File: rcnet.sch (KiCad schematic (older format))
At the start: 19 parts

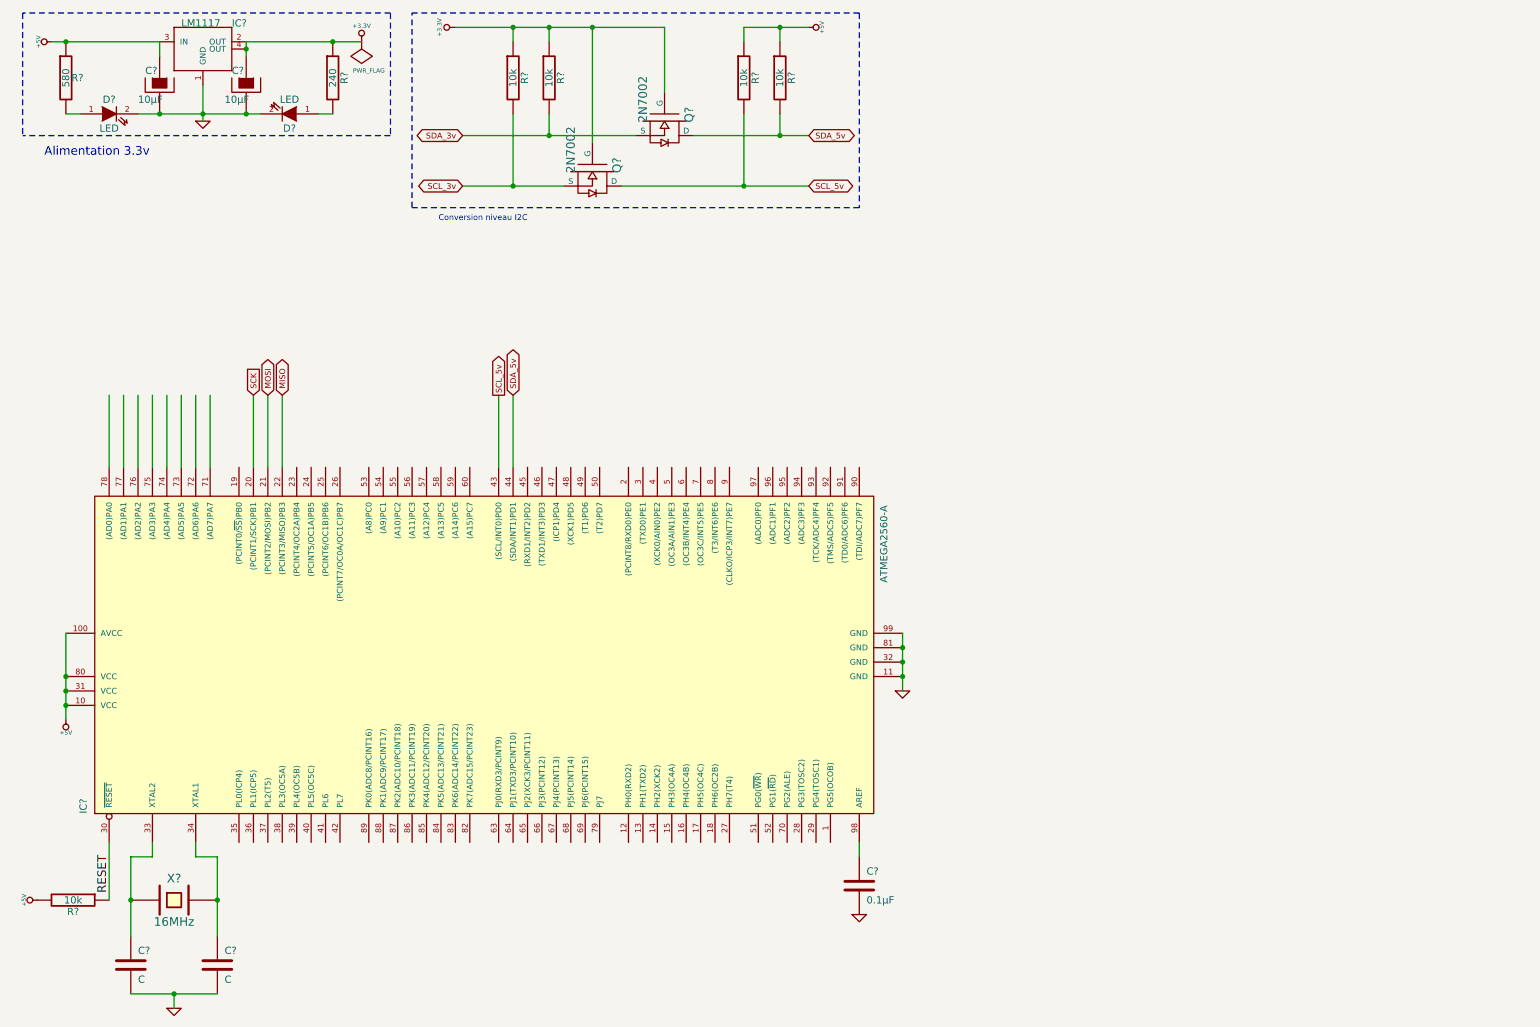
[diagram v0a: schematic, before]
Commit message: Ajout des capteurs I2C et cablage des MPU6050 et MS5611
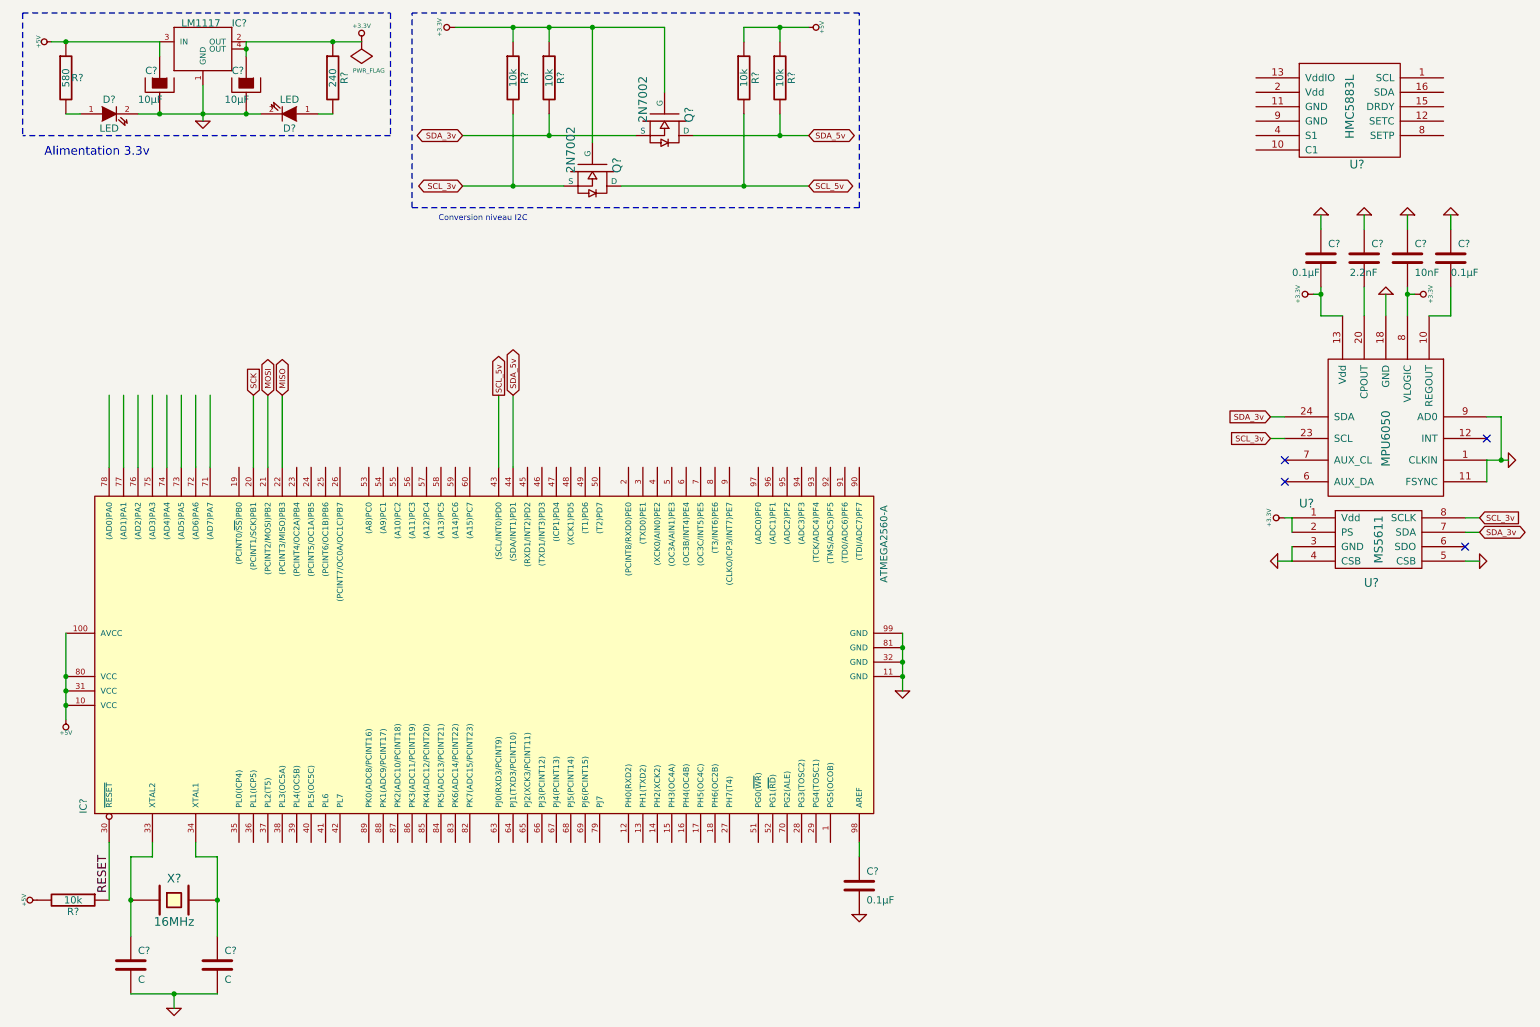
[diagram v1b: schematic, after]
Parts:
- added C?: 10nF, symbol C
- added C? (x2): 0.1µF, symbol C
- added C?: 2.2nF, symbol C
- added U?: HMC5883L, symbol HMC5883L
- added U?: MPU6050, symbol MPU6050
- added U?: MS5611, symbol MS5611
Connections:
- wire segments 49 -> 75
- no-connect marks 0 -> 4

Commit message: Fin d'ajout capteurs I2C.
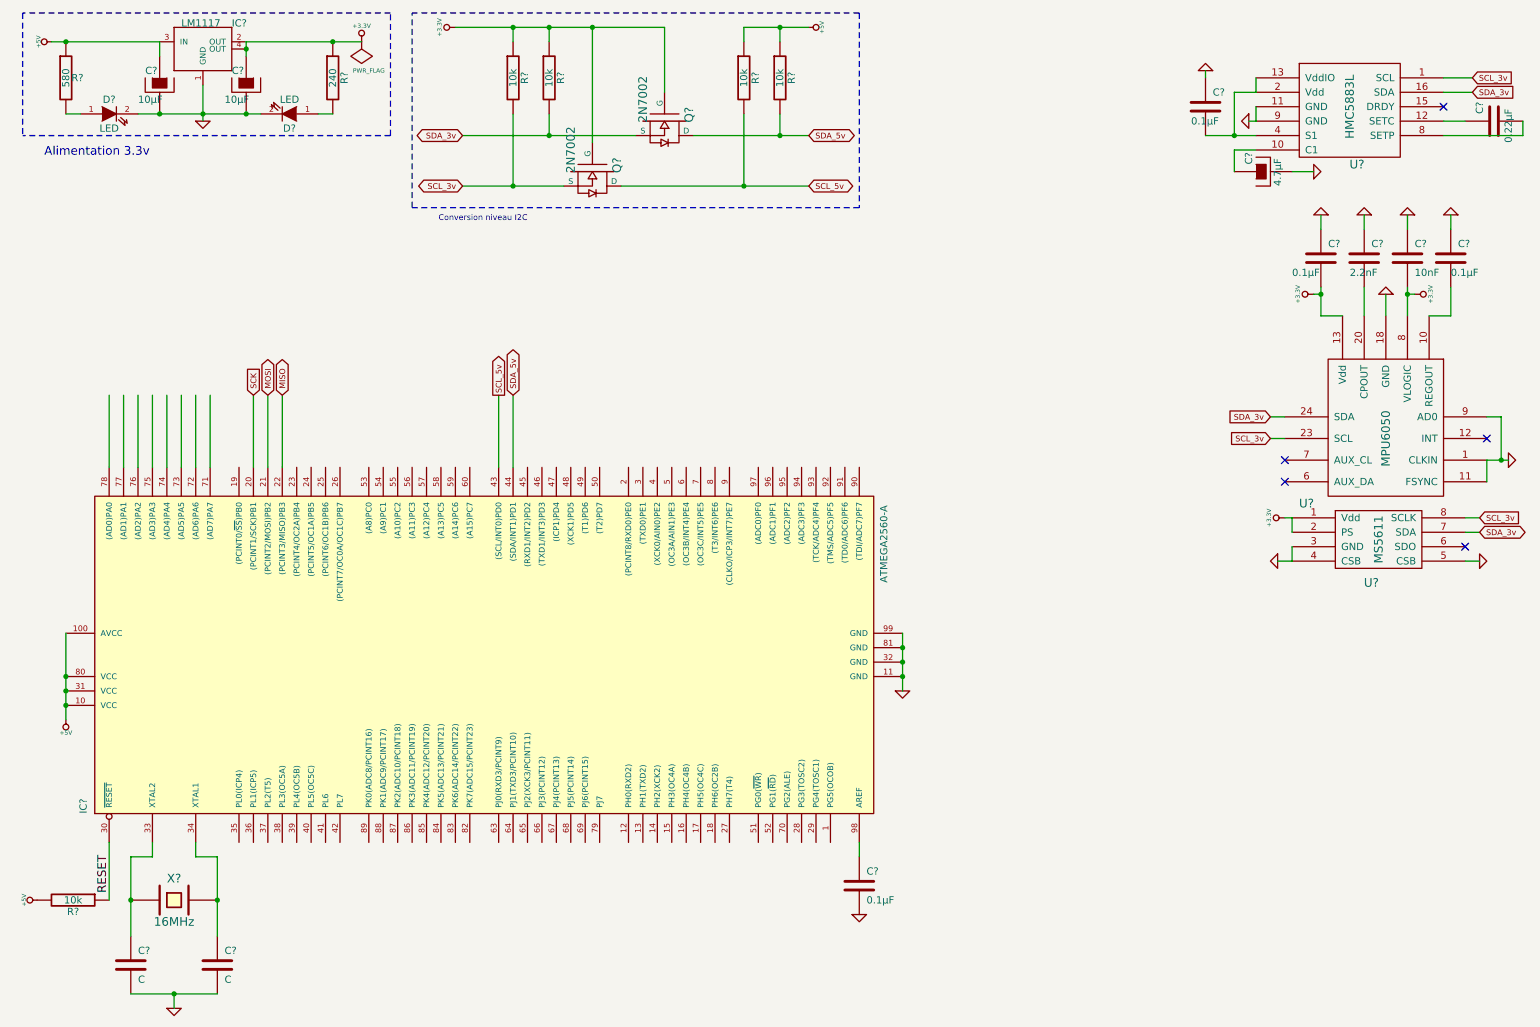
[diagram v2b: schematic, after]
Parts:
- added C?: 0.22µF, symbol C
- added C?: 0.1µF, symbol C
- added C?: 4.7µF, symbol CAPAPOL
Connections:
- wire segments 75 -> 90
- no-connect marks 4 -> 5

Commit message: Ajout des connecteurs FTDI/ICSP, cablage des entrées Rx et sorties PWM
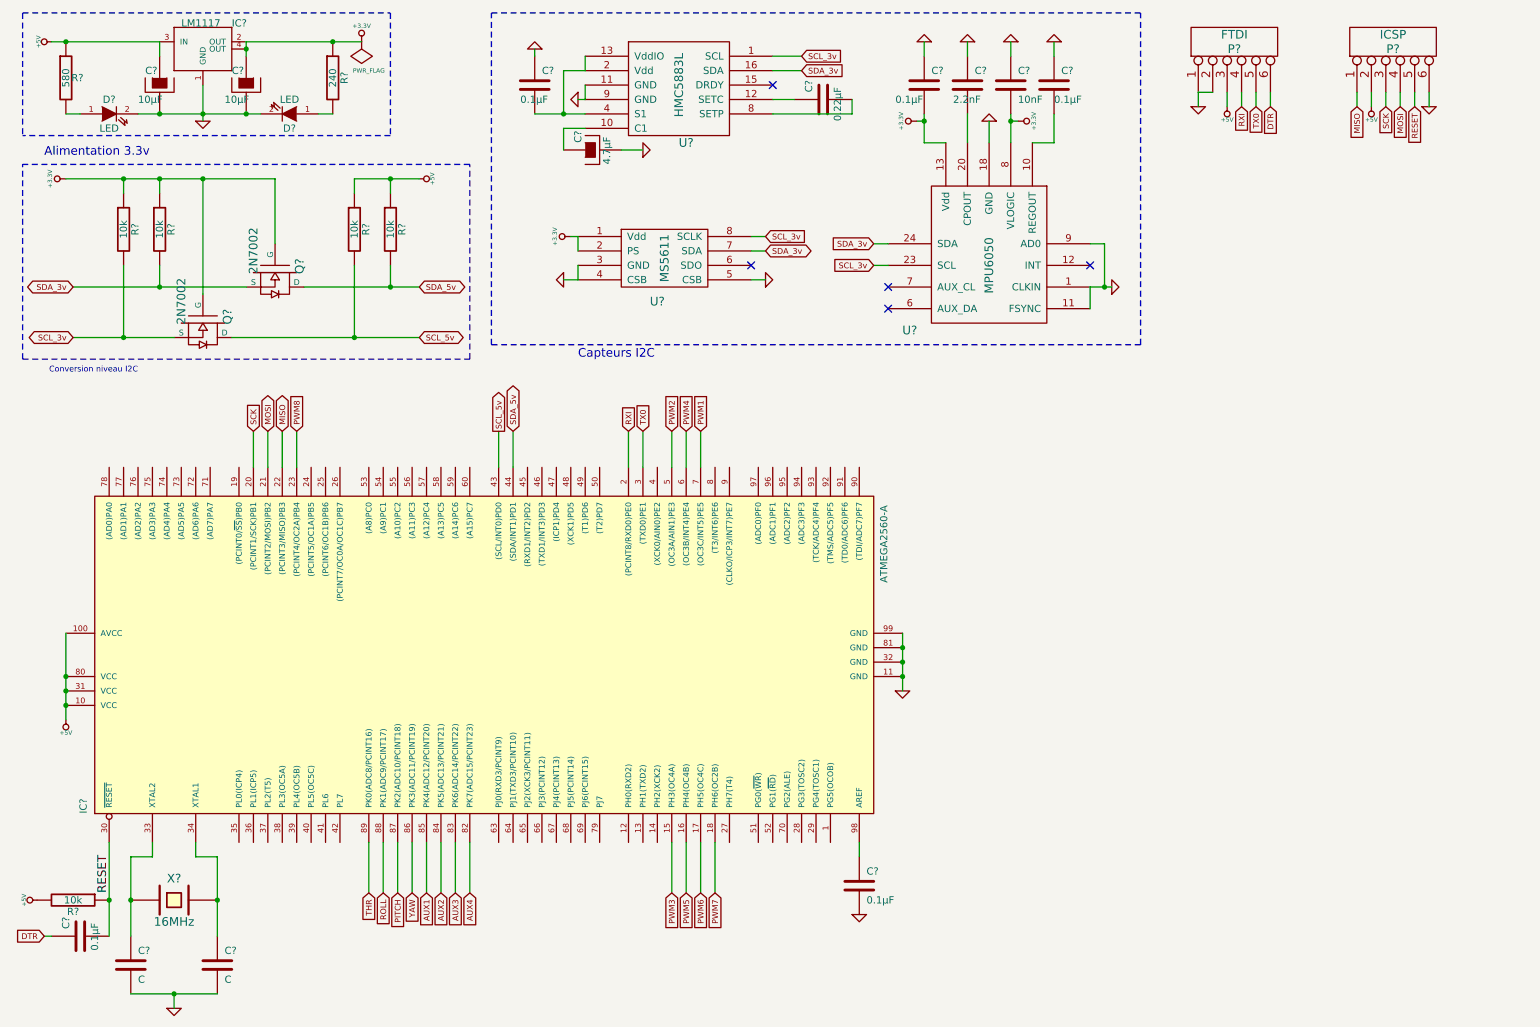
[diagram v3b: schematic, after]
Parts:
- added C?: 0.1µF, symbol C
- added P?: FTDI, symbol CONN_6
- added P?: ICSP, symbol CONN_6
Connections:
- net labels added: AUX1, AUX2, AUX3, AUX4, DTR, PITCH, PWM1, PWM2, PWM3, PWM4, PWM5, PWM6, PWM7, PWM8, ROLL, RXI, THR, TX0, YAW
- wire segments 90 -> 113
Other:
- note added: "Capteurs I2C"
- moved on the sheet: C?, Q?, R?, U?

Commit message: Cablage des I/O
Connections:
- net FLED: now reaches IC?.26 ((PCINT7/OC0A/OC1C)PB7)
- net PPM_INT: now reaches IC?.45 ((RXD1/INT2)PD2)
- net BUZZER: now reaches IC?.58 ((A13)PC5)
- net STABLE: now reaches IC?.59 ((A14)PC6)
- net SENSOR: now reaches IC?.95 ((ADC2)PF2)
- net VBAT: now reaches IC?.97 ((ADC0)PF0)
- no-connect marks 5 -> 20
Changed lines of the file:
@@
-EESchema Schematic File Version 2  date 28/07/2012 22:45:26
+EESchema Schematic File Version 2  date 29/07/2012 00:23:05
 LIBS:power
 LIBS:device
@@
 Comment4 ""
 $EndDescr
+NoConn ~ 5000 3800
+NoConn ~ 5500 3800
+NoConn ~ 5400 3800
+NoConn ~ 6100 6400
+NoConn ~ 6000 6400
+NoConn ~ 5500 6400
+NoConn ~ 4500 3800
+NoConn ~ 4400 3800
+NoConn ~ 4300 3800
+NoConn ~ 4600 6400
+NoConn ~ 4500 6400
+NoConn ~ 4400 6400
+NoConn ~ 4300 6400
+NoConn ~ 4200 6400
+NoConn ~ 4100 6400
+Wire Wire Line
+	5900 3550 5900 3800
+Wire Wire Line
+	4100 3550 4100 3800
+Wire Wire Line
+	3500 3550 3500 3800
 Wire Wire Line
 	10350 1200 10350 1300
@@
 Wire Wire Line
 	10250 1200 10250 1300
+Wire Wire Line
+	2800 3800 2800 3550
+Wire Wire Line
+	5700 3550 5700 3800
+Wire Wire Line
+	3600 3800 3600 3550
+Text GLabel 5900 3550 1    40   Input ~ 0
+SENSOR
+Text GLabel 3600 3550 1    40   Input ~ 0
+STABLE
+Text GLabel 4100 3550 1    40   Input ~ 0
+PPM_INT
+Text GLabel 5700 3550 1    40   Input ~ 0
+VBAT
+Text GLabel 3500 3550 1    40   Input ~ 0
+BUZZER
+Text GLabel 2800 3550 1    40   Input ~ 0
+FLED
 $Comp
 L GND #PWR?
